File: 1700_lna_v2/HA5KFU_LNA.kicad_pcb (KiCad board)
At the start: 4 copper layers, 35.8 x 15.2 mm, 19 parts, among them J1 Conn_Coaxial, J2 Conn_Coaxial, J3 571-1-826629-2, U1 NCP163ASN330T1G, U2 QPL9547

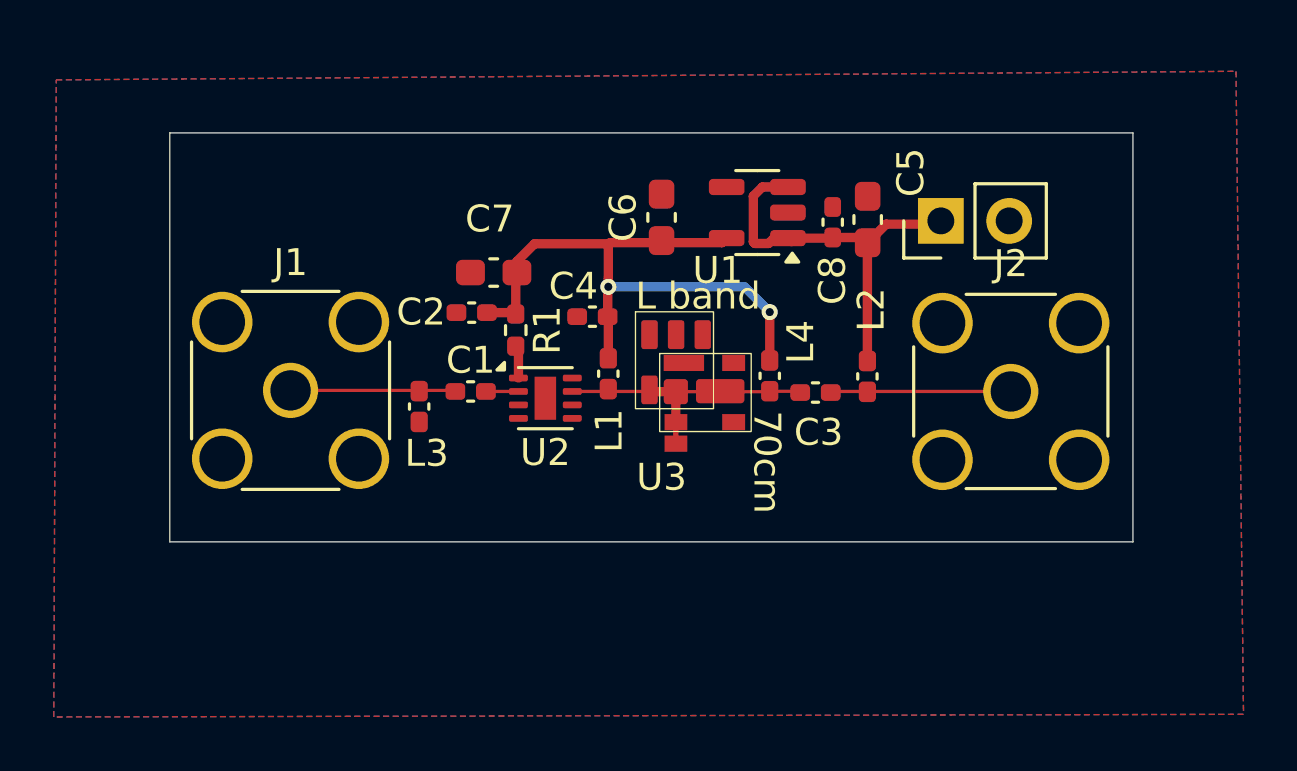
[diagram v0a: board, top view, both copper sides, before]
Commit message: Added extra vias and power source selector
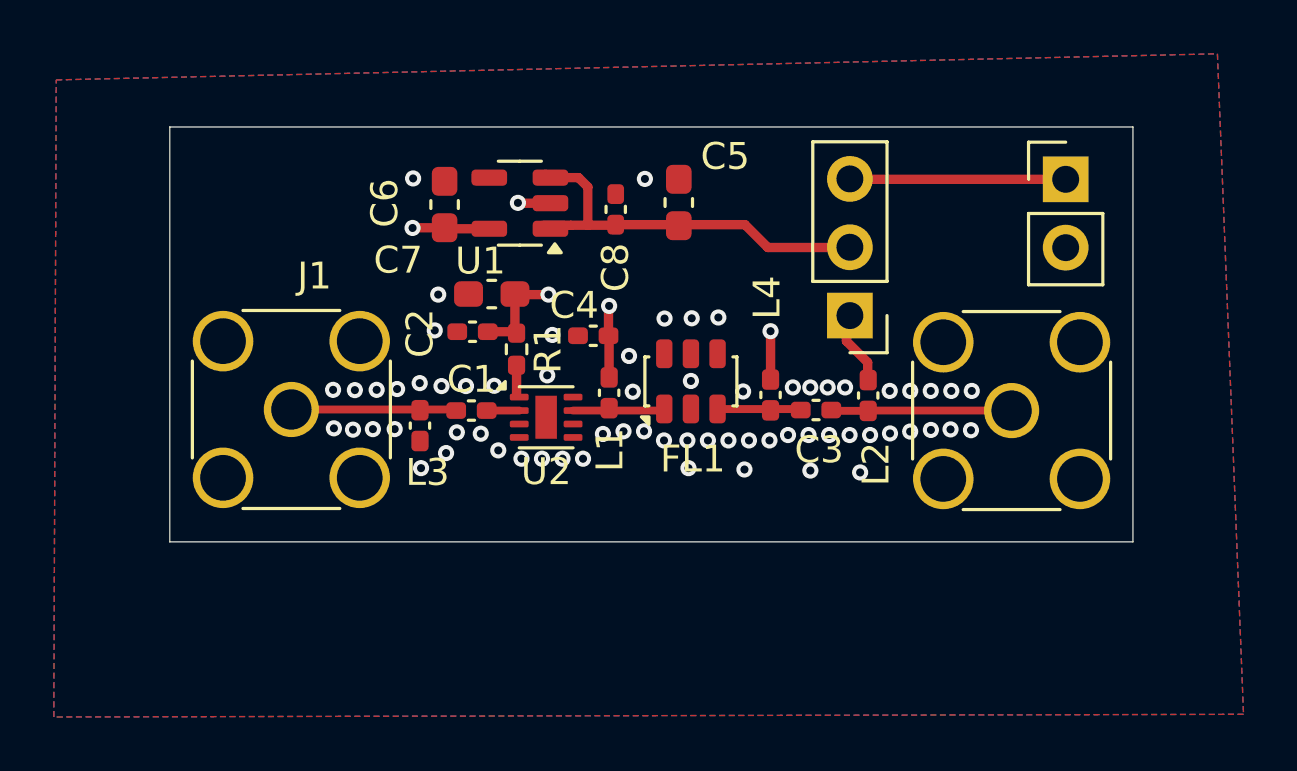
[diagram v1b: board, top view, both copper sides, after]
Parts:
- removed U3: ~, SAW_filt2:Combined
- added FL1: BFCN-1690, Filter:Filter_Mini-Circuits_FV1206-1, F.Cu at (132.6, 80.2)
- added J4: Conn_01x03_Pin, Connector_PinHeader_2.54mm:PinHeader_1x03_P2.54mm_Vertical, F.Cu at (138.5, 77.7)
- J2: footprint Connector_Coaxial:SMA_Amphenol_132291_Vertical -> Connector_Coaxial:SMA_Amphenol_132134_Vertical
- moved U1 8.83 mm to (126.3, 73.5)
- moved C6 8.08 mm to (123.5, 73.6)
- moved C8 8.08 mm to (129.8, 73.8)
- moved C5 7.05 mm to (132.2, 73.5)
- moved J3 4.89 mm to (146.6, 72.7), turned to 0 degrees
- moved C7 0.80 mm to (125.2, 76.9)
- moved L1 0.71 mm to (129.6, 80.6)
- moved L3 0.71 mm to (122.6, 81.8)
- moved L4 0.71 mm to (135.6, 80.7)
- moved C1 0.71 mm to (124.5, 81.2)
- moved C2 0.71 mm to (124.5, 78.3)
- moved C4 0.71 mm to (129.0, 78.5)
- moved J1 0.71 mm to (117.8, 81.2)
- moved J2 0.71 mm to (144.6, 81.2)
- moved L2 0.71 mm to (139.2, 80.7)
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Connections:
- C3 pad 1: Net-(U3-RFin/BFCN) -> Net-(FL1-OUT)
- C5 pad 1: +5V -> Net-(J4-Pin_2)
- C8 pad 2: +5V -> Net-(J4-Pin_2)
- L1 pad 2: Net-(U3-RFin/BFCN) -> Net-(FL1-IN)
- L2 pad 2: +5V -> Net-(J4-Pin_1)
- L4 pad 2: Net-(U3-RFin/BFCN) -> Net-(FL1-OUT)
- U1 pad 1: +5V -> Net-(J4-Pin_2)
- U1 pad 3: +5V -> Net-(J4-Pin_2)
- U2 pad 7: Net-(U3-RFin/BFCN) -> Net-(FL1-IN)
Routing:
- net Net-(J4-Pin_2): track 0.00 -> 15.0 mm
- net +3V3: track 23.7 -> 11.4 mm, vias 2 -> 4
- net Net-(U3-RFin/BFCN): track 10.1 -> 0.00 mm
- net +5V: track 15.3 -> 8.03 mm
- net Net-(FL1-IN): track 0.00 -> 3.54 mm
- net Net-(FL1-OUT): track 0.00 -> 3.24 mm
- net Net-(J4-Pin_1): track 0.00 -> 2.79 mm
- net GND: track 0.00 -> 1.22 mm, vias 0 -> 67
- added copper zone on In2.Cu, net +3V3
- added copper zone on In1.Cu, net GND
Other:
- board size 35.8 x 15.2 mm -> 35.8 x 15.4 mm

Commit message: refactor(lna_v2): prettify stitching vias
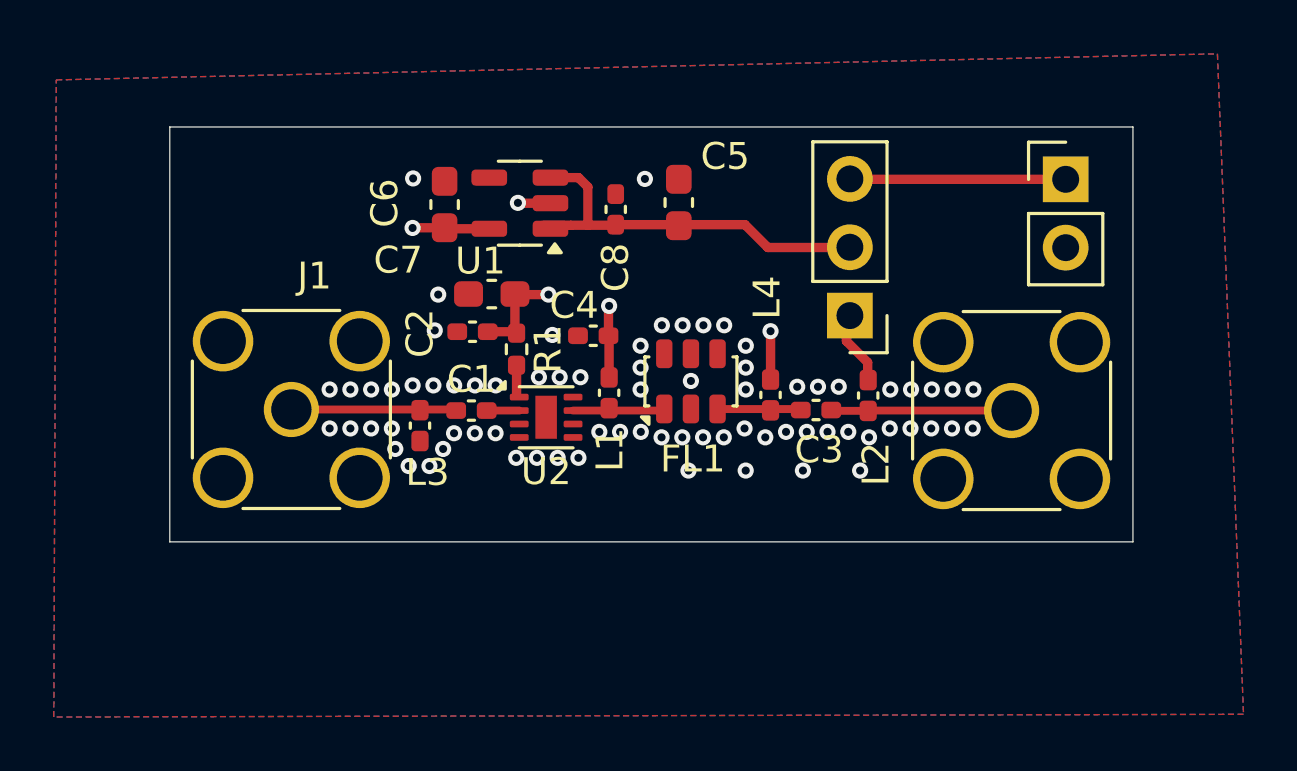
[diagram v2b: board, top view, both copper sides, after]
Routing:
- net GND: vias 67 -> 75
